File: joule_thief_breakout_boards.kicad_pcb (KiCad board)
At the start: 2 copper layers, 20.3 x 41.4 mm, 13 parts, among them J1 Conn_01x02, J2 Conn_01x02, J3 Conn_01x02, J4 Conn_01x02, J5 Conn_01x02, J6 Conn_01x03, J7 Conn_01x03, U1 INA180

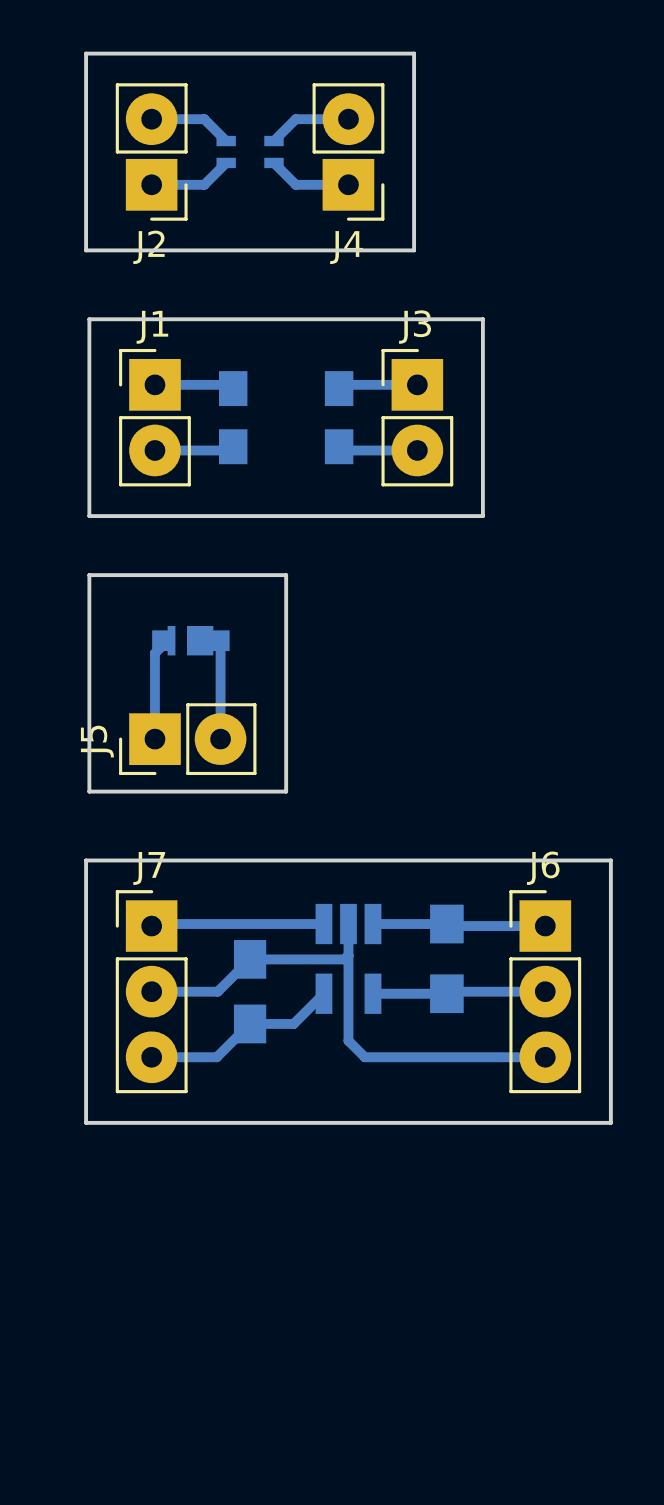
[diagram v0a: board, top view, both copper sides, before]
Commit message: transistor breakout pcb layout
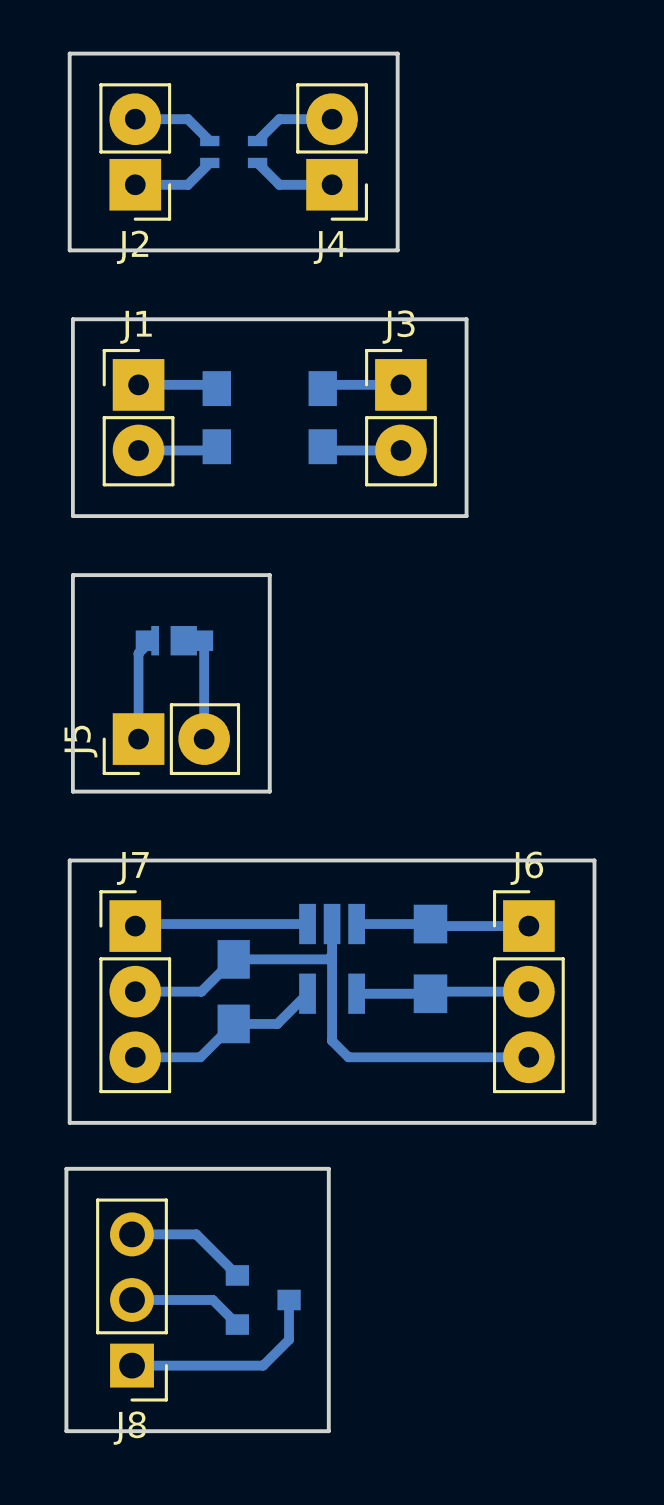
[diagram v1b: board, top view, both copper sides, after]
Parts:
- added J8: Conn_01x03, Pin_Headers:Pin_Header_Straight_1x03_Pitch2.54mm, F.Cu at (142.2, 146.1)
- added Q1: BC817-40, TO_SOT_Packages_SMD:SOT-23, B.Cu at (147.3, 143.5)
- moved C1 0.64 mm to (146.2, 131.6)
- moved D1 0.64 mm to (143.5, 118.0)
- moved FL2 0.64 mm to (146.2, 99.1)
- moved J2 0.64 mm to (142.4, 100.3)
- moved J4 0.64 mm to (150.0, 100.3)
- moved J7 0.64 mm to (142.4, 129.0)
- moved U1 0.64 mm to (150.0, 130.3)
- moved FL1 0.63 mm to (147.6, 109.3)
- moved J1 0.63 mm to (142.5, 108.1)
- moved J3 0.63 mm to (152.7, 108.1)
- moved J5 0.63 mm to (142.5, 121.8)
- moved J6 0.63 mm to (157.6, 129.0)
- moved R1 0.63 mm to (153.8, 130.3)
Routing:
- net Net-(J8-Pad1): track 0.00 -> 8.03 mm
- net Net-(J8-Pad3): track 0.00 -> 4.74 mm
- net Net-(J8-Pad2): track 0.00 -> 4.47 mm
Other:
- board size 20.3 x 41.4 mm -> 20.4 x 53.3 mm

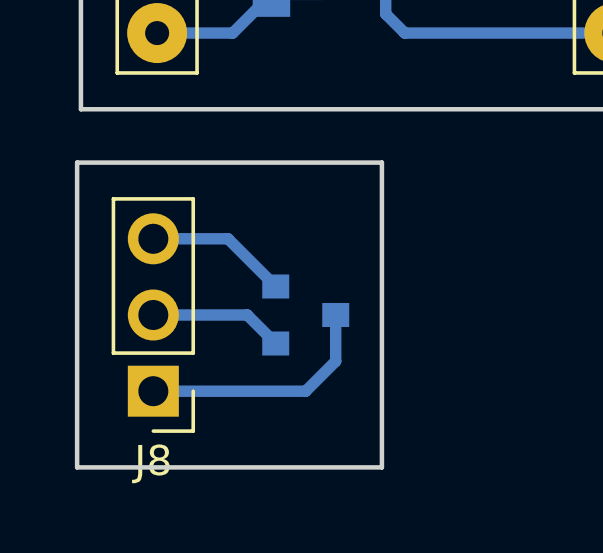
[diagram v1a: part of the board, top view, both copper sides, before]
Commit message: changed header for transistor footprint to custom etch footprint
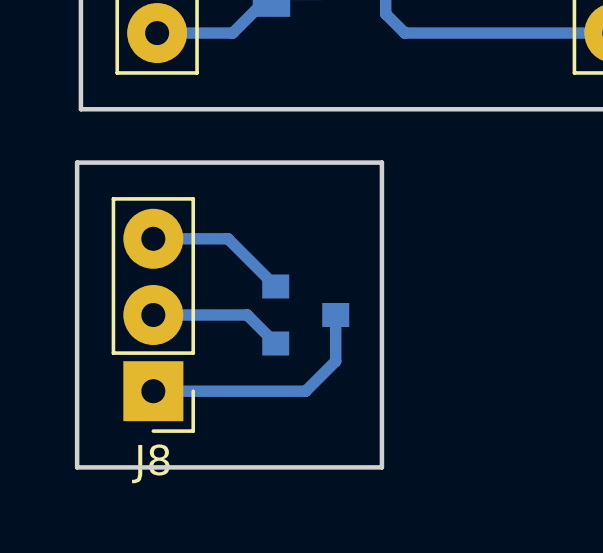
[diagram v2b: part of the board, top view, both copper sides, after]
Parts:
- J8: footprint Pin_Headers:Pin_Header_Straight_1x03_Pitch2.54mm -> lib_fp:Etch_Pin_Header_Straight_1x03_Pitch2.54mm
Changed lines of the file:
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@@
     (links 25)
     (no_connects 0)
-    (area 140.386999 95.174999 160.857001 136.727001)
+    (area 137.492381 94.485 162.35462 149.455)
     (thickness 1.6)
     (drawings 20)
@@
   )
   (setup
-    (last_trace_width 0.381)
+    (last_trace_width 0.25)
     (user_trace_width 0.381)
     (trace_clearance 0.2)
@@
       (drillshape 1)
       (scaleselection 1)
-      (outputdirectory ""))
+      (outputdirectory images/))
   )
   (net 0 "")
@@
       (net 8 "Net-(FL1-Pad4)"))
   )
-  (module Pin_Headers:Pin_Header_Straight_1x03_Pitch2.54mm (layer F.Cu)
-    (at 142.24 146.05 180)
-    (descr "Through hole straight pin header, 1x03, 2.54mm pitch, single row")
-    (tags "Through hole pin header THT 1x03 2.54mm single row")
-    (fp_text reference J8 (at 0 -2.33 180) (layer F.SilkS)
-      (effects (font (size 1 1) (thickness 0.15)))
-    )
-    (fp_text value Conn_01x03 (at 0 7.41 180) (layer F.Fab)
-      (effects (font (size 1 1) (thickness 0.15)))
-    )
-    (fp_line (start -0.635 -1.27) (end 1.27 -1.27) (layer F.Fab) (width 0.1))
-    (fp_line (start 1.27 -1.27) (end 1.27 6.35) (layer F.Fab) (width 0.1))
-    (fp_line (start 1.27 6.35) (end -1.27 6.35) (layer F.Fab) (width 0.1))
-    (fp_line (start -1.27 6.35) (end -1.27 -0.635) (layer F.Fab) (width 0.1))
-    (fp_line (start -1.27 -0.635) (end -0.635 -1.27) (layer F.Fab) (width 0.1))
-    (fp_line (start -1.33 6.41) (end 1.33 6.41) (layer F.SilkS) (width 0.12))
-    (fp_line (start -1.33 1.27) (end -1.33 6.41) (layer F.SilkS) (width 0.12))
-    (fp_line (start 1.33 1.27) (end 1.33 6.41) (layer F.SilkS) (width 0.12))
-    (fp_line (start -1.33 1.27) (end 1.33 1.27) (layer F.SilkS) (width 0.12))
-    (fp_line (start -1.33 0) (end -1.33 -1.33) (layer F.SilkS) (width 0.12))
-    (fp_line (start -1.33 -1.33) (end 0 -1.33) (layer F.SilkS) (width 0.12))
-    (fp_line (start -1.8 -1.8) (end -1.8 6.85) (layer F.CrtYd) (width 0.05))
-    (fp_line (start -1.8 6.85) (end 1.8 6.85) (layer F.CrtYd) (width 0.05))
-    (fp_line (start 1.8 6.85) (end 1.8 -1.8) (layer F.CrtYd) (width 0.05))
-    (fp_line (start 1.8 -1.8) (end -1.8 -1.8) (layer F.CrtYd) (width 0.05))
-    (fp_text user %R (at 0 2.54 270) (layer F.Fab)
-      (effects (font (size 1 1) (thickness 0.15)))
-    )
-    (pad 1 thru_hole rect (at 0 0 180) (size 1.7 1.7) (drill 1) (layers *.Cu *.Mask)
-      (net 16 "Net-(J8-Pad1)"))
-    (pad 2 thru_hole oval (at 0 2.54 180) (size 1.7 1.7) (drill 1) (layers *.Cu *.Mask)
-      (net 17 "Net-(J8-Pad2)"))
-    (pad 3 thru_hole oval (at 0 5.08 180) (size 1.7 1.7) (drill 1) (layers *.Cu *.Mask)
-      (net 18 "Net-(J8-Pad3)"))
-    (model ${KISYS3DMOD}/Pin_Headers.3dshapes/Pin_Header_Straight_1x03_Pitch2.54mm.wrl
-      (at (xyz 0 0 0))
-      (scale (xyz 1 1 1))
-      (rotate (xyz 0 0 0))
-    )
-  )
   (module TO_SOT_Packages_SMD:SOT-23 (layer B.Cu)
     (at 147.32 143.51)
@@
       (at (xyz 0 0 0))
       (scale (xyz 1 1 1))
+      (rotate (xyz 0 0 0))
+    )
+  )
+  (module lib_fp:Etch_Pin_Header_Straight_1x03_Pitch2.54mm (layer F.Cu)
+    (at 142.24 146.05 180)
+    (descr "Through hole straight pin header, 1x03, 2.54mm pitch, single row")
+    (tags "Through hole pin header THT 1x03 2.54mm single row")
+    (fp_text reference J8 (at 0 -2.33 180) (layer F.SilkS)
+      (effects (font (size 1 1) (thickness 0.15)))
+    )
+    (fp_text value Conn_01x03 (at 0 7.41 180) (layer F.Fab)
+      (effects (font (size 1 1) (thickness 0.15)))
+    )
+    (fp_line (start -0.635 -1.27) (end 1.27 -1.27) (layer F.Fab) (width 0.1))
+    (fp_line (start 1.27 -1.27) (end 1.27 6.35) (layer F.Fab) (width 0.1))
+    (fp_line (start 1.27 6.35) (end -1.27 6.35) (layer F.Fab) (width 0.1))
+    (fp_line (start -1.27 6.35) (end -1.27 -0.635) (layer F.Fab) (width 0.1))
+    (fp_line (start -1.27 -0.635) (end -0.635 -1.27) (layer F.Fab) (width 0.1))
+    (fp_line (start -1.33 6.41) (end 1.33 6.41) (layer F.SilkS) (width 0.12))
+    (fp_line (start -1.33 1.27) (end -1.33 6.41) (layer F.SilkS) (width 0.12))
+    (fp_line (start 1.33 1.27) (end 1.33 6.41) (layer F.SilkS) (width 0.12))
+    (fp_line (start -1.33 1.27) (end 1.33 1.27) (layer F.SilkS) (width 0.12))
+    (fp_line (start -1.33 0) (end -1.33 -1.33) (layer F.SilkS) (width 0.12))
+    (fp_line (start -1.33 -1.33) (end 0 -1.33) (layer F.SilkS) (width 0.12))
+    (fp_line (start -1.8 -1.8) (end -1.8 6.85) (layer F.CrtYd) (width 0.05))
+    (fp_line (start -1.8 6.85) (end 1.8 6.85) (layer F.CrtYd) (width 0.05))
+    (fp_line (start 1.8 6.85) (end 1.8 -1.8) (layer F.CrtYd) (width 0.05))
+    (fp_line (start 1.8 -1.8) (end -1.8 -1.8) (layer F.CrtYd) (width 0.05))
+    (fp_text user %R (at 0 2.54 270) (layer F.Fab)
+      (effects (font (size 1 1) (thickness 0.15)))
+    )
+    (pad 1 thru_hole rect (at 0 0 180) (size 2 2) (drill 0.8) (layers *.Cu *.Mask)
+      (net 16 "Net-(J8-Pad1)"))
+    (pad 2 thru_hole oval (at 0 2.54 180) (size 2 2) (drill 0.8) (layers *.Cu *.Mask)
+      (net 17 "Net-(J8-Pad2)"))
+    (pad 3 thru_hole oval (at 0 5.08 180) (size 2 2) (drill 0.8) (layers *.Cu *.Mask)
+      (net 18 "Net-(J8-Pad3)"))
+    (model ${KISYS3DMOD}/Pin_Headers.3dshapes/Pin_Header_Straight_1x03_Pitch2.54mm.wrl
+      (at (xyz 0 0 0))
+      (scale (xyz 1 1 1))
